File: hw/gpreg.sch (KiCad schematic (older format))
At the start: 2 parts

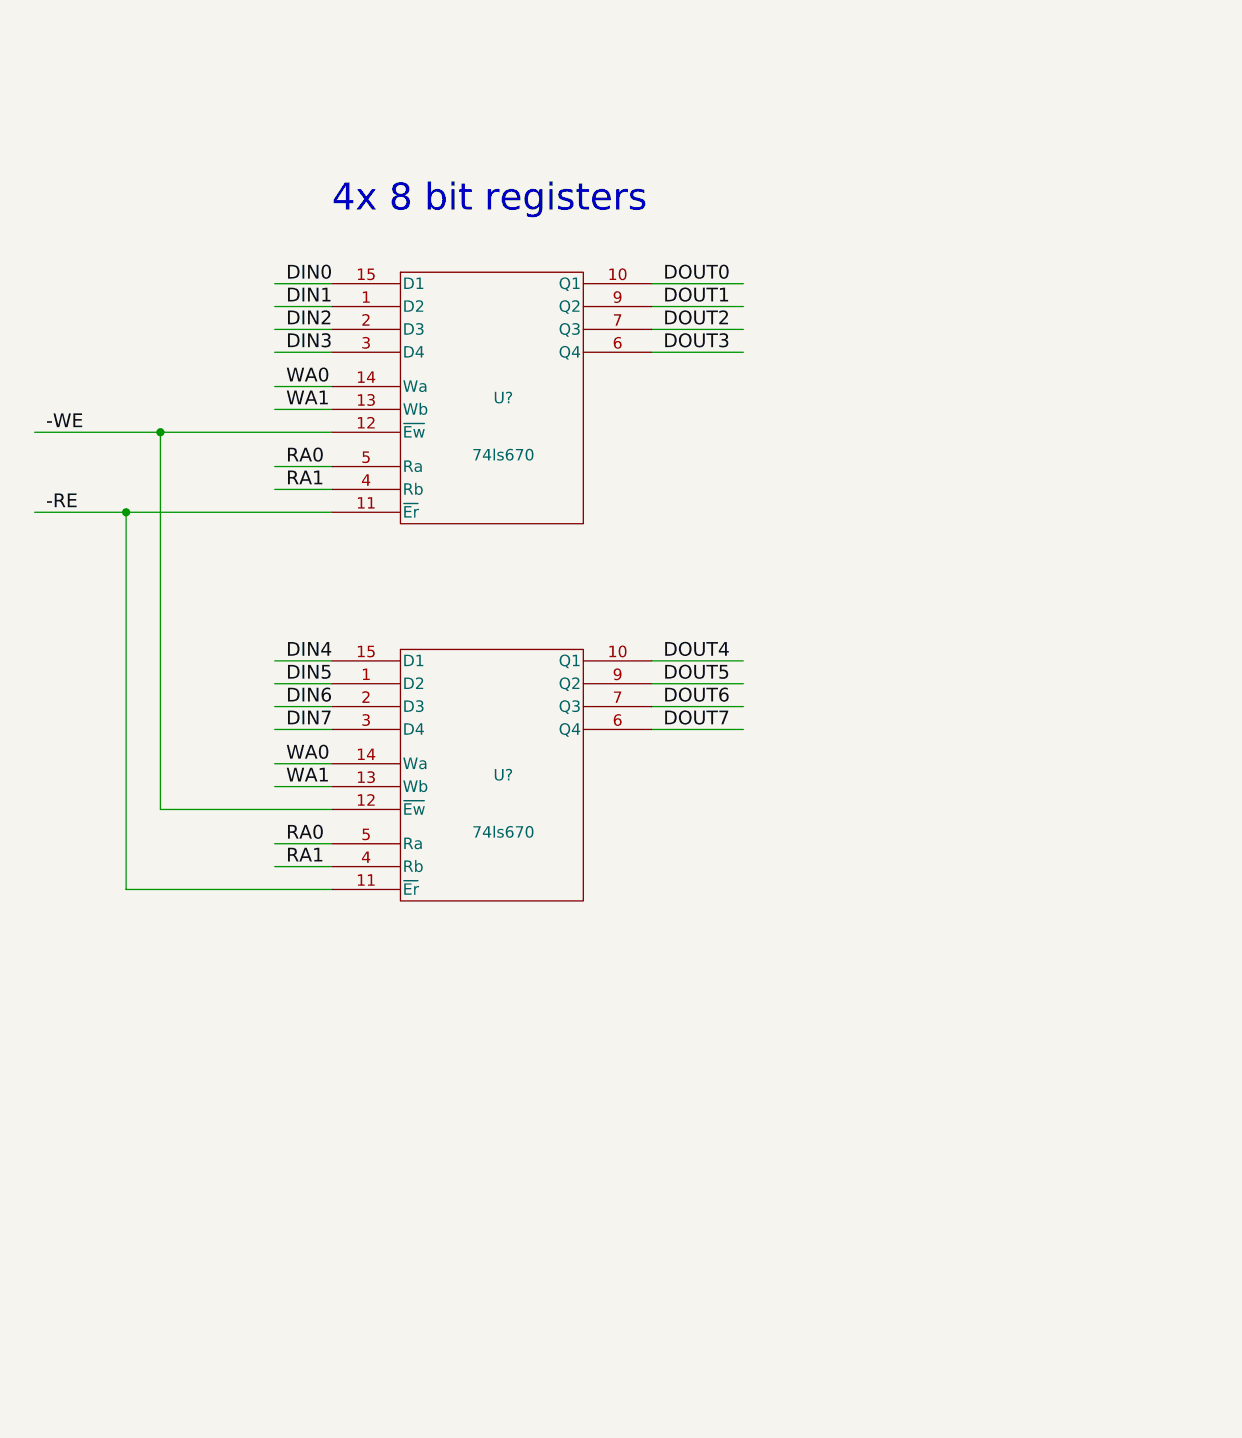
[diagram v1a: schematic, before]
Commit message: implement GP registers
Also, add ucode signals to main sheet, and do
some cleanup on main sheet.
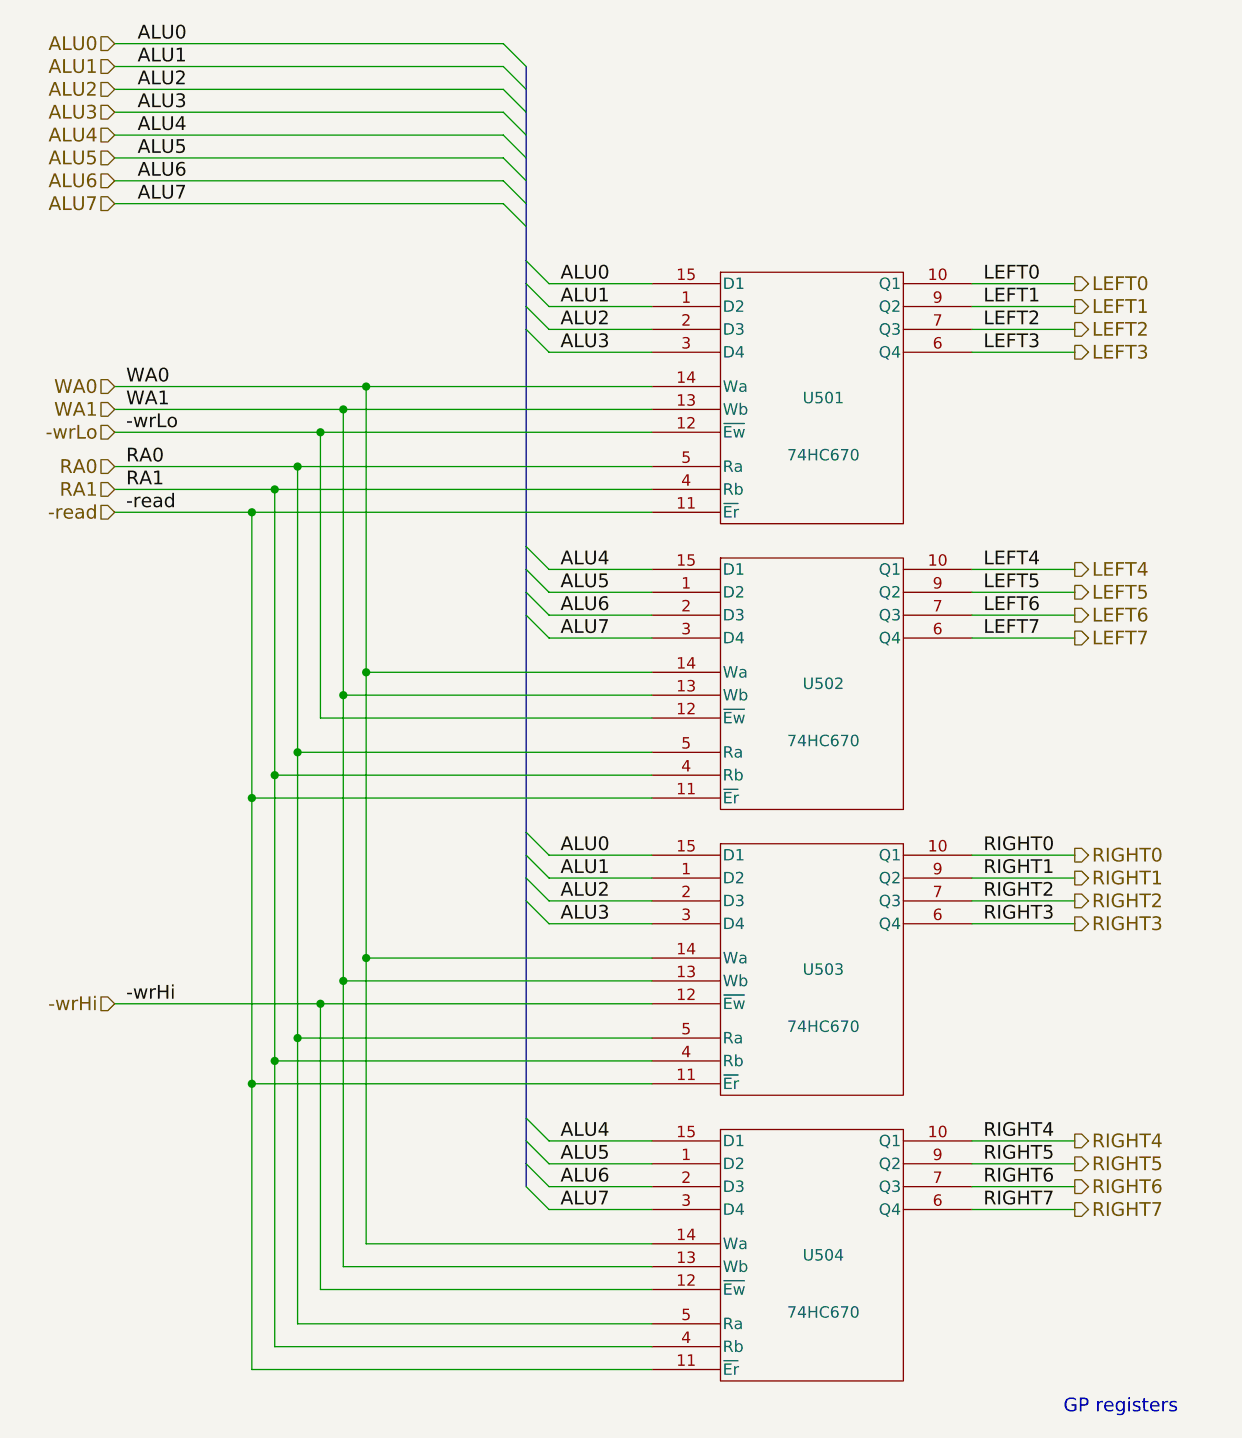
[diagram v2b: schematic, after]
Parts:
- added U503, U504: 74HC670, symbol 74ls670
- U501, U502: renamed from U?; value 74ls670 -> 74HC670
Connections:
- net labels added: -read, -wrHi, -wrLo, ALU0, ALU1, ALU2, ALU3, ALU4, ALU5, ALU6, ALU7, LEFT0, LEFT1, LEFT2, LEFT3, LEFT4, LEFT5, LEFT6, LEFT7, RIGHT0, RIGHT1, RIGHT2, RIGHT3, RIGHT4, RIGHT5, RIGHT6, RIGHT7
- net labels removed: -RE, -WE, DIN0, DIN1, DIN2, DIN3, DIN4, DIN5, DIN6, DIN7, DOUT0, DOUT1, DOUT2, DOUT3, DOUT4, DOUT5, DOUT6, DOUT7
- wire segments 30 -> 88
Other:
- note added: "GP registers"
- note removed: "4x 8 bit registers"
- moved on the sheet: U501, U502
